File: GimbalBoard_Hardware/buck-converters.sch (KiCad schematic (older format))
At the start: 20 parts, among them U1 OKI, U2 OKI, U3 OKI, U4 OKI

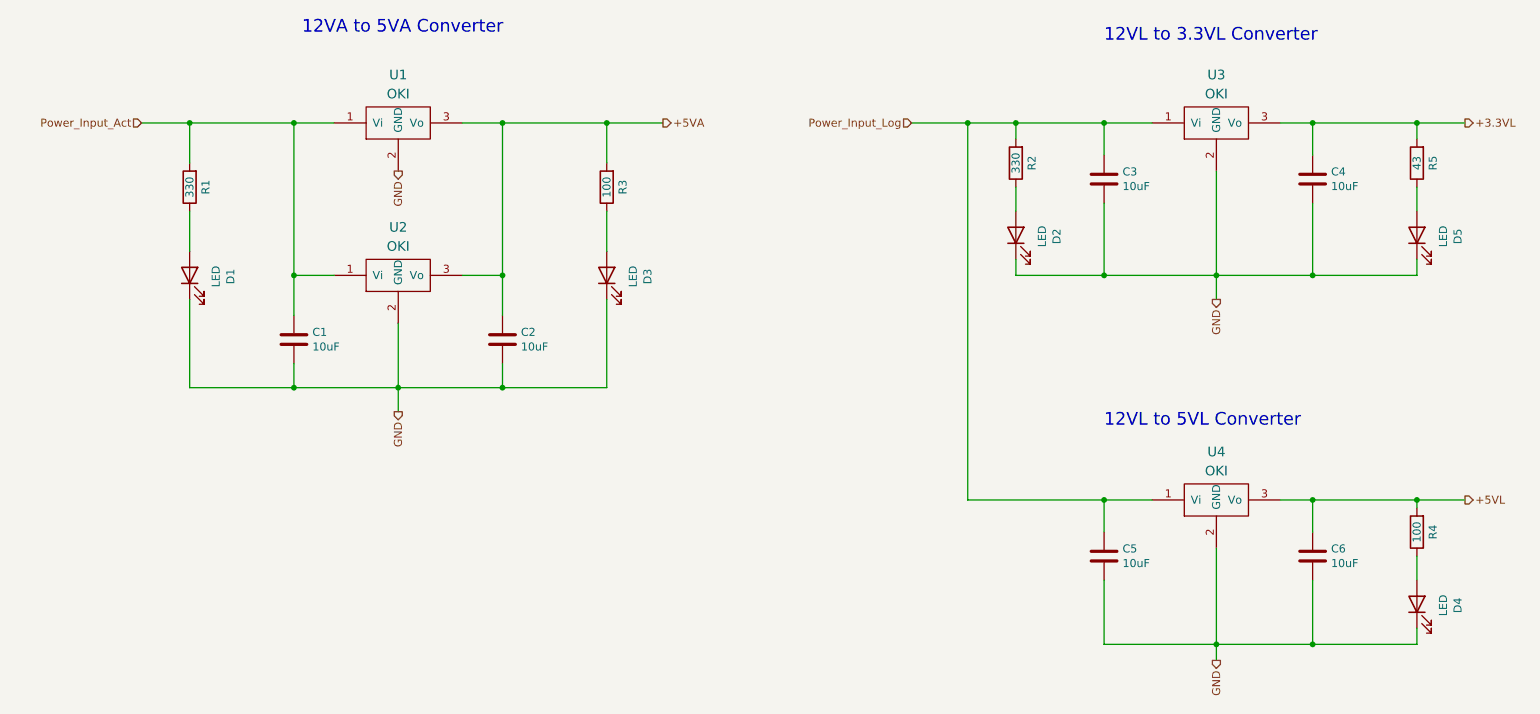
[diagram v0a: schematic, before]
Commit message: now powering the teensy w 3.3VL instead of 5VL
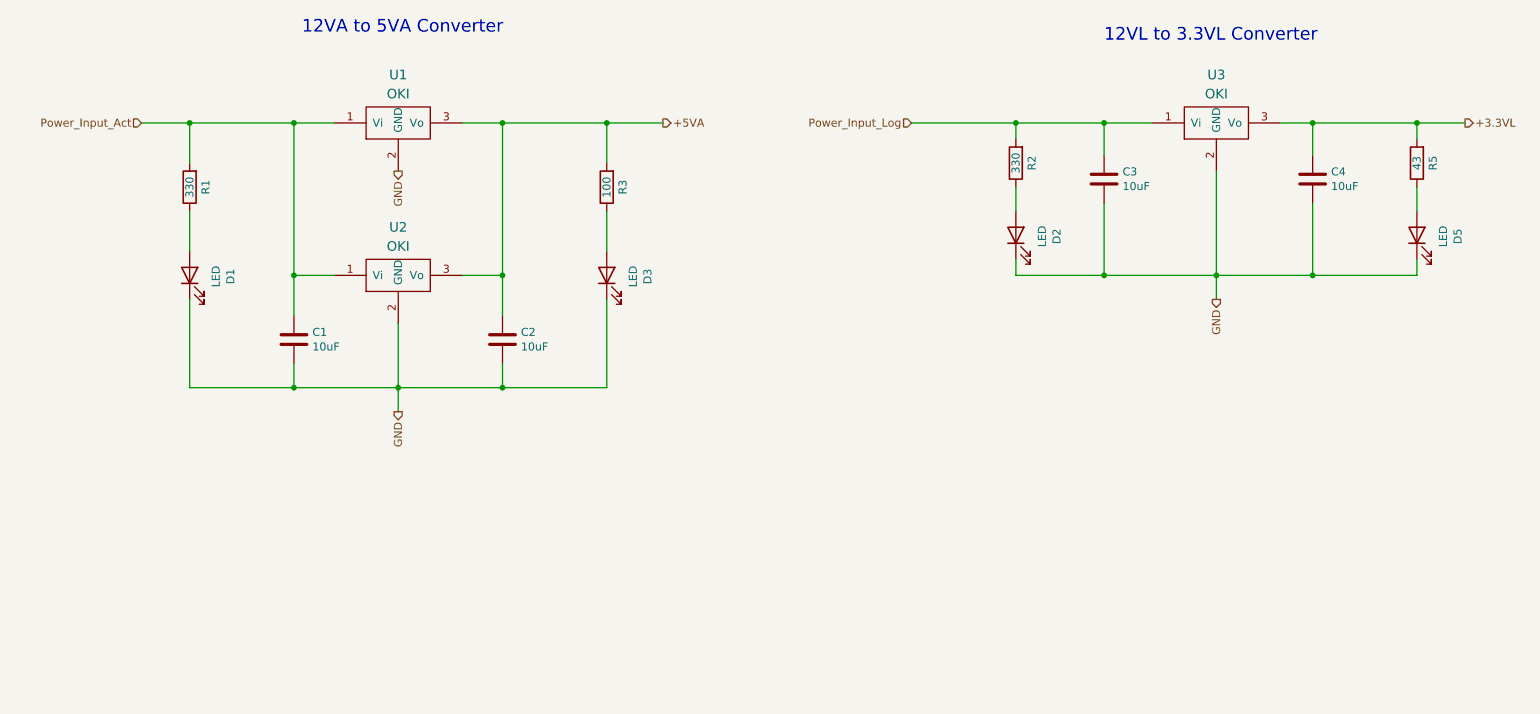
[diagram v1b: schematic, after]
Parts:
- removed C5, C6: 10uF, symbol Device:C
- removed D4: LED, symbol Device:LED
- removed R4: 100, symbol Device:R
- removed U4: OKI, symbol MRDT_Devices:OKI
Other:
- note removed: "12VL to 5VL Converter"
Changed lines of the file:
@@
 $Descr A4 11693 8268
 encoding utf-8
-Sheet 3 5
+Sheet 5 5
 Title ""
 Date ""
@@
 Text HLabel 1400 1750 0    50   Input ~ 0
 Power_Input_Act
-Wire Wire Line
-	8500 4100 8700 4100
-Wire Wire Line
-	8700 4300 8700 4100
-Wire Wire Line
-	8100 5000 8700 5000
-Connection ~ 8100 5000
-Wire Wire Line
-	7400 5000 8100 5000
-Wire Wire Line
-	7400 4100 7700 4100
-Wire Wire Line
-	7400 4100 7400 4300
-Text HLabel 9650 4100 2    50   Output ~ 0
-+5VL
-$Comp
-L MRDT_Devices:OKI U?
-U 1 1 616BE8BC
-P 7900 4200
-AR Path="/616BE8BC" Ref="U?"  Part="1"
-AR Path="/615B83A4/616BE8BC" Ref="U?"  Part="1"
-AR Path="/6160709D/616BE8BC" Ref="U?"  Part="1"
-AR Path="/616B938E/616BE8BC" Ref="U4"  Part="1"
-F 0 "U4" H 8100 4600 60  0000 C CNN
-F 1 "OKI" H 8100 4481 60  0000 C CNN
-F 2 "" H 7700 4100 60  0001 C CNN
-F 3 "" H 7700 4100 60  0001 C CNN
-	1    7900 4200
-	1    0    0    -1
-$EndComp
-$Comp
-L Device:C C?
-U 1 1 616BE8C2
-P 8700 4450
-AR Path="/616BE8C2" Ref="C?"  Part="1"
-AR Path="/615B83A4/616BE8C2" Ref="C?"  Part="1"
-AR Path="/6160709D/616BE8C2" Ref="C?"  Part="1"
-AR Path="/616B938E/616BE8C2" Ref="C6"  Part="1"
-F 0 "C6" H 8815 4496 50  0000 L CNN
-F 1 "10uF" H 8815 4405 50  0000 L CNN
-F 2 "" H 8738 4300 50  0001 C CNN
-F 3 "~" H 8700 4450 50  0001 C CNN
-	1    8700 4450
-	1    0    0    -1
-$EndComp
-$Comp
-L Device:C C?
-U 1 1 616BE8C8
-P 7400 4450
-AR Path="/616BE8C8" Ref="C?"  Part="1"
-AR Path="/615B83A4/616BE8C8" Ref="C?"  Part="1"
-AR Path="/6160709D/616BE8C8" Ref="C?"  Part="1"
-AR Path="/616B938E/616BE8C8" Ref="C5"  Part="1"
-F 0 "C5" H 7515 4496 50  0000 L CNN
-F 1 "10uF" H 7515 4405 50  0000 L CNN
-F 2 "" H 7438 4300 50  0001 C CNN
-F 3 "~" H 7400 4450 50  0001 C CNN
-	1    7400 4450
-	1    0    0    -1
-$EndComp
 Wire Wire Line
 	8500 1750 8700 1750
@@
 	1    0    0    -1
 $EndComp
-Connection ~ 7400 4100
 Text Notes 7400 1250 0    79   ~ 0
 12VL to 3.3VL Converter
-Text Notes 7400 3650 0    79   ~ 0
-12VL to 5VL Converter
 Text HLabel 6200 1750 0    50   Input ~ 0
 Power_Input_Log
-Text HLabel 8100 5100 3    50   Output ~ 0
-GND
 Text HLabel 8100 2850 3    50   Output ~ 0
 GND
@@
 $EndComp
 $Comp
-L Device:LED D?
-U 1 1 616C1771
-P 9350 4750
-AR Path="/61616981/616C1771" Ref="D?"  Part="1"
-AR Path="/616B938E/616C1771" Ref="D4"  Part="1"
-F 0 "D4" H 9343 4495 50  0000 C CNN
-F 1 "LED" H 9343 4586 50  0000 C CNN
-F 2 "" H 9350 4750 50  0001 C CNN
-F 3 "~" H 9350 4750 50  0001 C CNN
-	1    9350 4750
-	0    -1   -1   0
-$EndComp
-$Comp
 L Device:R R?
 U 1 1 616C177D
@@
 F 3 "~" H 4300 2150 50  0001 C CNN
 	1    4300 2150
-	-1   0    0    1
-$EndComp
-$Comp
-L Device:R R?
-U 1 1 616C1789
-P 9350 4300
-AR Path="/61616981/616C1789" Ref="R?"  Part="1"
-AR Path="/616B938E/616C1789" Ref="R4"  Part="1"
-F 0 "R4" V 9250 4300 50  0000 C CNN
-F 1 "100" V 9350 4300 50  0000 C CNN
-F 2 "" V 9280 4300 50  0001 C CNN
-F 3 "~" H 9350 4300 50  0001 C CNN
-	1    9350 4300
 	-1   0    0    1
 $EndComp
@@
 	9350 1750 9350 1850
 Wire Wire Line
-	8700 4100 9350 4100
-Connection ~ 8700 4100
-Wire Wire Line
-	9350 4100 9350 4150
-Connection ~ 9350 4100
-Wire Wire Line
-	9350 4450 9350 4600
-Wire Wire Line
-	8700 5000 9350 5000
-Wire Wire Line
-	9350 5000 9350 4900
-Connection ~ 8700 5000
-Wire Wire Line
-	8700 4600 8700 5000
-Wire Wire Line
-	8100 4400 8100 5000
-Wire Wire Line
-	7400 4600 7400 5000
-Wire Wire Line
-	8100 5000 8100 5100
-Wire Wire Line
-	6550 1750 6550 4100
-Wire Wire Line
-	6550 1750 6850 1750
-Wire Wire Line
-	6550 4100 7400 4100
-Wire Wire Line
-	6200 1750 6550 1750
-Connection ~ 6550 1750
-Wire Wire Line
-	9350 4100 9650 4100
+	6200 1750 6850 1750
 $EndSCHEMATC

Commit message: footprints added
some footprints have been added but only a few
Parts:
- C1, C2, C3, C4: footprint (none) -> Capacitor_SMD:C_0603_1608Metric_Pad1.08x0.95mm_HandSolder
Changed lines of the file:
@@
 F 0 "C4" H 8815 2146 50  0000 L CNN
 F 1 "10uF" H 8815 2055 50  0000 L CNN
-F 2 "" H 8738 1950 50  0001 C CNN
+F 2 "Capacitor_SMD:C_0603_1608Metric_Pad1.08x0.95mm_HandSolder" H 8738 1950 50  0001 C CNN
 F 3 "~" H 8700 2100 50  0001 C CNN
 	1    8700 2100
@@
 F 0 "C3" H 7515 2146 50  0000 L CNN
 F 1 "10uF" H 7515 2055 50  0000 L CNN
-F 2 "" H 7438 1950 50  0001 C CNN
+F 2 "Capacitor_SMD:C_0603_1608Metric_Pad1.08x0.95mm_HandSolder" H 7438 1950 50  0001 C CNN
 F 3 "~" H 7400 2100 50  0001 C CNN
 	1    7400 2100
@@
 F 0 "C1" H 2465 3146 50  0000 L CNN
 F 1 "10uF" H 2465 3055 50  0000 L CNN
-F 2 "" H 2388 2950 50  0001 C CNN
+F 2 "Capacitor_SMD:C_0603_1608Metric_Pad1.08x0.95mm_HandSolder" H 2388 2950 50  0001 C CNN
 F 3 "~" H 2350 3100 50  0001 C CNN
 	1    2350 3100
@@
 F 0 "C2" H 3765 3146 50  0000 L CNN
 F 1 "10uF" H 3765 3055 50  0000 L CNN
-F 2 "" H 3688 2950 50  0001 C CNN
+F 2 "Capacitor_SMD:C_0603_1608Metric_Pad1.08x0.95mm_HandSolder" H 3688 2950 50  0001 C CNN
 F 3 "~" H 3650 3100 50  0001 C CNN
 	1    3650 3100

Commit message: Added more footprints
I added more footprints. Not done yet. I'd like to come back when when I can verify with max about some of the other components.
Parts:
- D1, D2, D3, D5: footprint (none) -> LED_SMD:LED_0603_1608Metric_Pad1.05x0.95mm_HandSolder
- R1, R2, R3, R5: footprint (none) -> Resistor_SMD:R_0603_1608Metric_Pad0.98x0.95mm_HandSolder
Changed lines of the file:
@@
 F 0 "D2" H 6843 2195 50  0000 C CNN
 F 1 "LED" H 6843 2286 50  0000 C CNN
-F 2 "" H 6850 2450 50  0001 C CNN
+F 2 "LED_SMD:LED_0603_1608Metric_Pad1.05x0.95mm_HandSolder" H 6850 2450 50  0001 C CNN
 F 3 "~" H 6850 2450 50  0001 C CNN
 	1    6850 2450
@@
 F 0 "D3" H 4293 2445 50  0000 C CNN
 F 1 "LED" H 4293 2536 50  0000 C CNN
-F 2 "" H 4300 2700 50  0001 C CNN
+F 2 "LED_SMD:LED_0603_1608Metric_Pad1.05x0.95mm_HandSolder" H 4300 2700 50  0001 C CNN
 F 3 "~" H 4300 2700 50  0001 C CNN
 	1    4300 2700
@@
 F 0 "R2" V 6750 2000 50  0000 C CNN
 F 1 "330" V 6850 2000 50  0000 C CNN
-F 2 "" V 6780 2000 50  0001 C CNN
+F 2 "Resistor_SMD:R_0603_1608Metric_Pad0.98x0.95mm_HandSolder" V 6780 2000 50  0001 C CNN
 F 3 "~" H 6850 2000 50  0001 C CNN
 	1    6850 2000
@@
 F 0 "R3" V 4200 2150 50  0000 C CNN
 F 1 "100" V 4300 2150 50  0000 C CNN
-F 2 "" V 4230 2150 50  0001 C CNN
+F 2 "Resistor_SMD:R_0603_1608Metric_Pad0.98x0.95mm_HandSolder" V 4230 2150 50  0001 C CNN
 F 3 "~" H 4300 2150 50  0001 C CNN
 	1    4300 2150
@@
 F 0 "D5" H 9343 2195 50  0000 C CNN
 F 1 "LED" H 9343 2286 50  0000 C CNN
-F 2 "" H 9350 2450 50  0001 C CNN
+F 2 "LED_SMD:LED_0603_1608Metric_Pad1.05x0.95mm_HandSolder" H 9350 2450 50  0001 C CNN
 F 3 "~" H 9350 2450 50  0001 C CNN
 	1    9350 2450
@@
 F 0 "R5" V 9250 2000 50  0000 C CNN
 F 1 "43" V 9350 2000 50  0000 C CNN
-F 2 "" V 9280 2000 50  0001 C CNN
+F 2 "Resistor_SMD:R_0603_1608Metric_Pad0.98x0.95mm_HandSolder" V 9280 2000 50  0001 C CNN
 F 3 "~" H 9350 2000 50  0001 C CNN
 	1    9350 2000
@@
 F 0 "D1" H 1693 2445 50  0000 C CNN
 F 1 "LED" H 1693 2536 50  0000 C CNN
-F 2 "" H 1700 2700 50  0001 C CNN
+F 2 "LED_SMD:LED_0603_1608Metric_Pad1.05x0.95mm_HandSolder" H 1700 2700 50  0001 C CNN
 F 3 "~" H 1700 2700 50  0001 C CNN
 	1    1700 2700
@@
 F 0 "R1" V 1600 2150 50  0000 C CNN
 F 1 "330" V 1700 2150 50  0000 C CNN
-F 2 "" V 1630 2150 50  0001 C CNN
+F 2 "Resistor_SMD:R_0603_1608Metric_Pad0.98x0.95mm_HandSolder" V 1630 2150 50  0001 C CNN
 F 3 "~" H 1700 2150 50  0001 C CNN
 	1    1700 2150

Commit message: Footprints finished
the footprints are finished. the RJ45 connector has been added for eithernet.
the net is in the layout thing but I haven't moved anything yet
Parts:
- U1, U2, U3: footprint (none) -> MRDT_Devices:OKI_Horizontal
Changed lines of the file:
@@
 F 0 "U3" H 8100 2250 60  0000 C CNN
 F 1 "OKI" H 8100 2131 60  0000 C CNN
-F 2 "" H 7700 1750 60  0001 C CNN
+F 2 "MRDT_Devices:OKI_Horizontal" H 7700 1750 60  0001 C CNN
 F 3 "" H 7700 1750 60  0001 C CNN
 	1    7900 1850
@@
 F 0 "U1" H 3000 2250 60  0000 C CNN
 F 1 "OKI" H 3000 2131 60  0000 C CNN
-F 2 "" H 2600 1750 60  0001 C CNN
+F 2 "MRDT_Devices:OKI_Horizontal" H 2600 1750 60  0001 C CNN
 F 3 "" H 2600 1750 60  0001 C CNN
 	1    2800 1850
@@
 F 0 "U2" H 3000 3200 60  0000 C CNN
 F 1 "OKI" H 3000 3081 60  0000 C CNN
-F 2 "" H 2600 2700 60  0001 C CNN
+F 2 "MRDT_Devices:OKI_Horizontal" H 2600 2700 60  0001 C CNN
 F 3 "" H 2600 2700 60  0001 C CNN
 	1    2800 2800
